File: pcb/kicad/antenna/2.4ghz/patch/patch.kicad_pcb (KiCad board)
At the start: 2 copper layers, 2 parts, among them P1 SMA

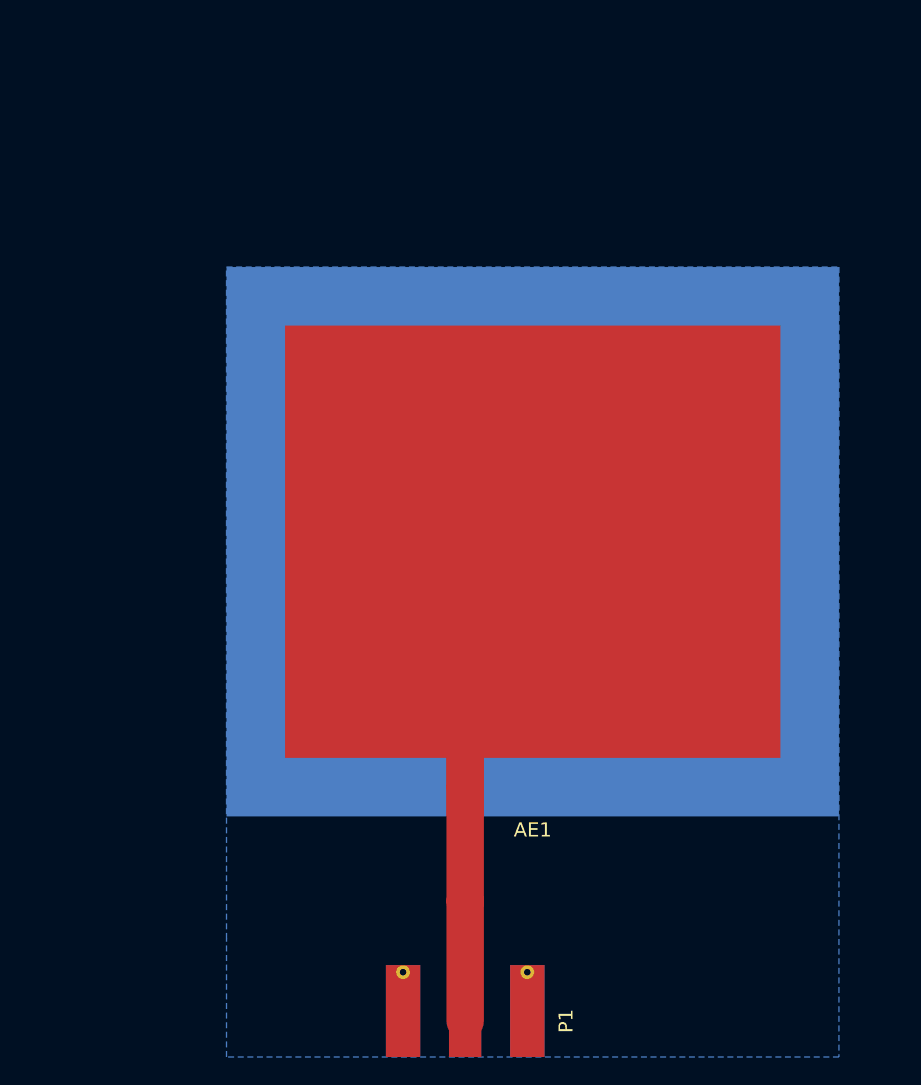
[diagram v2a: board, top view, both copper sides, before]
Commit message: Add new tests for patch antenna
Two new test boards laid out to test impedance and performance due to
the effect of larger copper void space in the presence of nearby ground
copper, one board with a matching circuit and the other without. Traces
no longer follow the optimal transmission line width for 50ohm
performance due to the use of 0402 SMD technology.
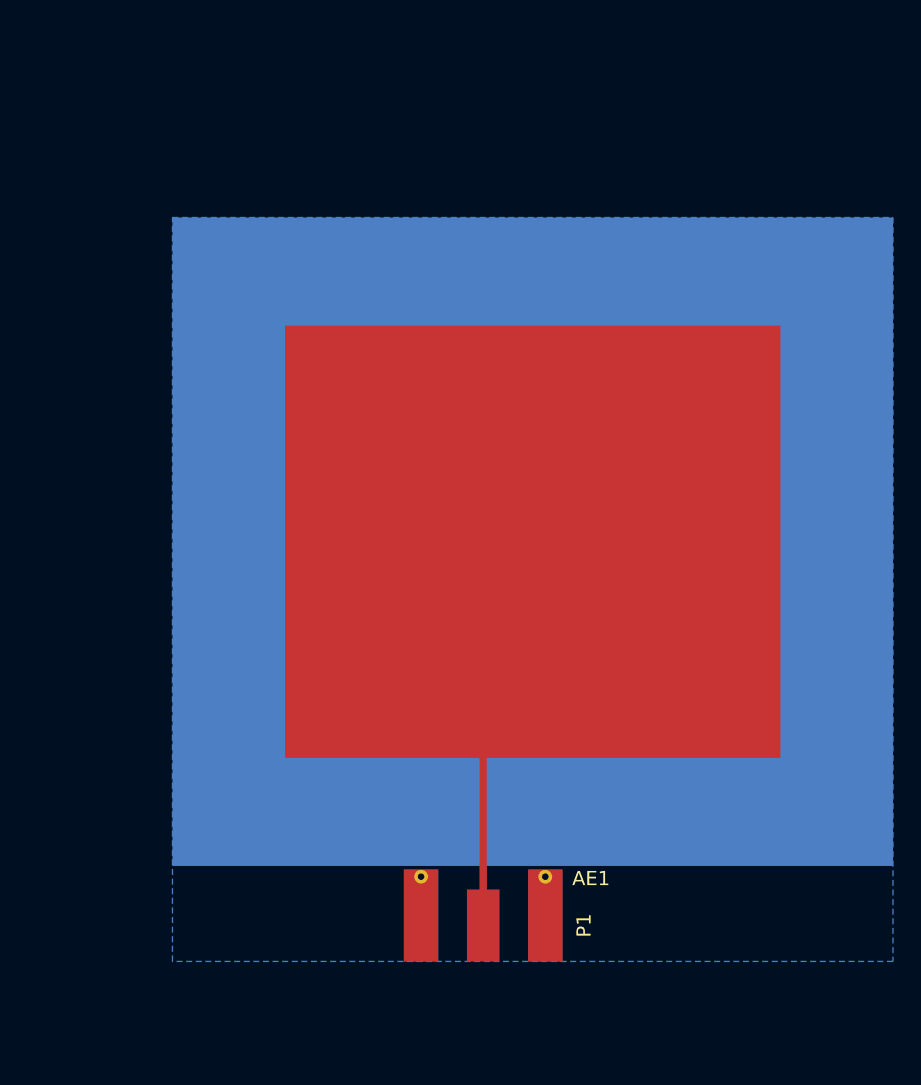
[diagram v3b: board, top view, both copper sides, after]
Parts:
- AE1: value Antenna -> Antenna_Shield
- moved P1 6.85 mm to (145.1, 114.2)
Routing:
- net /SIG: track 35.8 -> 28.5 mm
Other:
- net class Default: trace_width 2.6416 -> 0.508
- board text added: "April 4, 2017"
- board text removed: "March 15, 2017"
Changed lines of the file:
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@@
 (kicad_pcb (version 4) (host pcbnew 4.0.5)
   (general
-    (links 8)
+    (links 7)
     (no_connects 0)
-    (area 126.873 67.678 272.295714 194.39)
+    (area 0 0 0 0)
     (thickness 1.5748)
     (drawings 7)
-    (tracks 4)
+    (tracks 2)
     (zones 0)
     (modules 2)
@@
   )
   (setup
-    (last_trace_width 2.6416)
+    (last_trace_width 0.508)
     (trace_clearance 0.127)
     (zone_clearance 0.127)
@@
     (mod_text_size 1 1)
     (mod_text_width 0.15)
-    (pad_size 43.18 38.735)
+    (pad_size 34.925 30.48)
     (pad_drill 0)
     (pad_to_mask_clearance 0.2)
-    (aux_axis_origin 127 125.22962)
+    (aux_axis_origin 123.19 118.491)
     (visible_elements 7FFFFFFF)
     (pcbplotparams
@@
   (net_class Default "This is the default net class."
     (clearance 0.127)
-    (trace_width 2.6416)
+    (trace_width 0.508)
     (via_dia 0.3048)
     (via_drill 0.254)
@@
     (add_net GND)
   )
-  (module Antennas:Patch_Antenna_2.4GHz (layer F.Cu)
-    (at 148.59 88.9)
-    (descr "2.4GHz Patch Antenna")
-    (tags "antenna patch 2.4")
-    (fp_text reference AE1 (at 0 20.32) (layer F.SilkS)
-      (effects (font (size 1 1) (thickness 0.15)))
-    )
-    (fp_text value Antenna (at 0 -20.32) (layer F.Fab)
-      (effects (font (size 1 1) (thickness 0.15)))
-    )
-    (pad 2 smd rect (at 0 0) (size 43.18 38.735) (layers B.Cu)
-      (net 2 GND))
-    (pad 1 smd rect (at 0 0) (size 34.925 30.48) (layers F.Cu)
-      (net 1 /SIG))
-    (pad 1 smd rect (at -4.7625 17.30375) (size 2.6416 4.1275) (layers F.Cu)
-      (net 1 /SIG))
-  )
   (module Misc:Molex_SMA_Jack_Edge_Mount (layer F.Cu)
-    (at 143.8275 120.97004 90)
+    (at 145.0975 114.2365 90)
     (descr "Molex SMA Jack, Edge Mount")
     (tags "sma edge")
@@
       (net 2 GND) (zone_connect 2))
   )
-  (gr_line (start 170.18 69.5325) (end 127 69.5325) (angle 90) (layer Margin) (width 0.2))
-  (gr_line (start 170.18 125.22962) (end 170.18 69.5325) (angle 90) (layer Margin) (width 0.2))
-  (gr_line (start 127 125.22962) (end 170.18 125.22962) (angle 90) (layer Margin) (width 0.2))
-  (gr_line (start 127 69.5325) (end 127 125.22962) (angle 90) (layer Margin) (width 0.2))
-  (gr_text "March 15, 2017" (at 217.17 193.04) (layer Cmts.User)
+  (module Antennas:Patch_Antenna_2.4GHz (layer F.Cu)
+    (at 148.59 88.9)
+    (descr "2.4GHz Patch Antenna")
+    (tags "antenna patch 2.4")
+    (fp_text reference AE1 (at 4.1148 23.749) (layer F.SilkS)
+      (effects (font (size 1 1) (thickness 0.15)))
+    )
+    (fp_text value Antenna_Shield (at 0 -23.622) (layer F.Fab)
+      (effects (font (size 1 1) (thickness 0.15)))
+    )
+    (pad 2 smd rect (at 0 0) (size 50.8 45.72) (layers B.Cu)
+      (net 2 GND))
+    (pad 1 smd rect (at 0 0) (size 34.925 30.48) (layers F.Cu)
+      (net 1 /SIG))
+  )
+  (gr_line (start 173.99 66.04) (end 123.19 66.04) (angle 90) (layer Margin) (width 0.2))
+  (gr_line (start 173.99 118.491) (end 173.99 66.04) (angle 90) (layer Margin) (width 0.2))
+  (gr_line (start 123.19 118.491) (end 173.99 118.491) (angle 90) (layer Margin) (width 0.2))
+  (gr_line (start 123.19 66.04) (end 123.19 118.491) (angle 90) (layer Margin) (width 0.2))
+  (gr_text "April 4, 2017" (at 214.63 193.04) (layer Cmts.User)
     (effects (font (size 1.5 1.5) (thickness 0.3)))
   )
@@
     (effects (font (size 1.5 1.5) (thickness 0.3)))
   )
-  (segment (start 143.8275 122.69004) (end 143.8275 114.242) (width 2.6416) (layer F.Cu) (net 1) (status 400000))
-  (segment (start 143.8275 114.242) (end 143.8275 106.20375) (width 2.6416) (layer F.Cu) (net 1) (status 30))
-  (segment (start 143.8275 106.20375) (end 143.8275 93.6625) (width 2.6416) (layer F.Cu) (net 1) (status 30))
-  (segment (start 143.8275 93.6625) (end 148.59 88.9) (width 2.6416) (layer F.Cu) (net 1) (status 30))
+  (segment (start 145.0975 115.9565) (end 145.0975 92.3925) (width 0.508) (layer F.Cu) (net 1))
+  (segment (start 145.0975 92.3925) (end 148.59 88.9) (width 0.508) (layer F.Cu) (net 1))
   (zone (net 2) (net_name GND) (layer B.Cu) (hatch edge 0.508)
     (connect_pads thru_hole_only (clearance 0.127))
     (min_thickness 0.127)
-    (fill yes (arc_segments 32) (thermal_gap 0.508) (thermal_bridge_width 0.508))
+    (fill yes (arc_segments 16) (thermal_gap 0.508) (thermal_bridge_width 0.508))
     (polygon
       (pts
-        (xy 170.18 125.22962) (xy 127 125.22962) (xy 127 116.9035) (xy 127 69.5325) (xy 170.18 69.5325)
+        (xy 173.99 118.491) (xy 123.19 118.491) (xy 123.19 66.04) (xy 173.99 66.04)
       )
     )
-    (polygon
-      (pts        (xy 127 116.9035) (xy 127.00508 116.9162) (xy 127.00508 116.9035)
-      )
-    )

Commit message: Add gerbtool files for new patch tests
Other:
- board text added: "0.2.1"
- board text removed: "0.2"
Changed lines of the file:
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@@
     (links 7)
     (no_connects 0)
-    (area 0 0 0 0)
+    (area 123.063 64.376 272.295714 194.39)
     (thickness 1.5748)
     (drawings 7)
@@
     (effects (font (size 1.5 1.5) (thickness 0.3)))
   )
-  (gr_text 0.2 (at 270.51 193.04) (layer Cmts.User)
+  (gr_text 0.2.1 (at 271.78 193.04) (layer Cmts.User)
     (effects (font (size 1.5 1.5) (thickness 0.3)))
   )

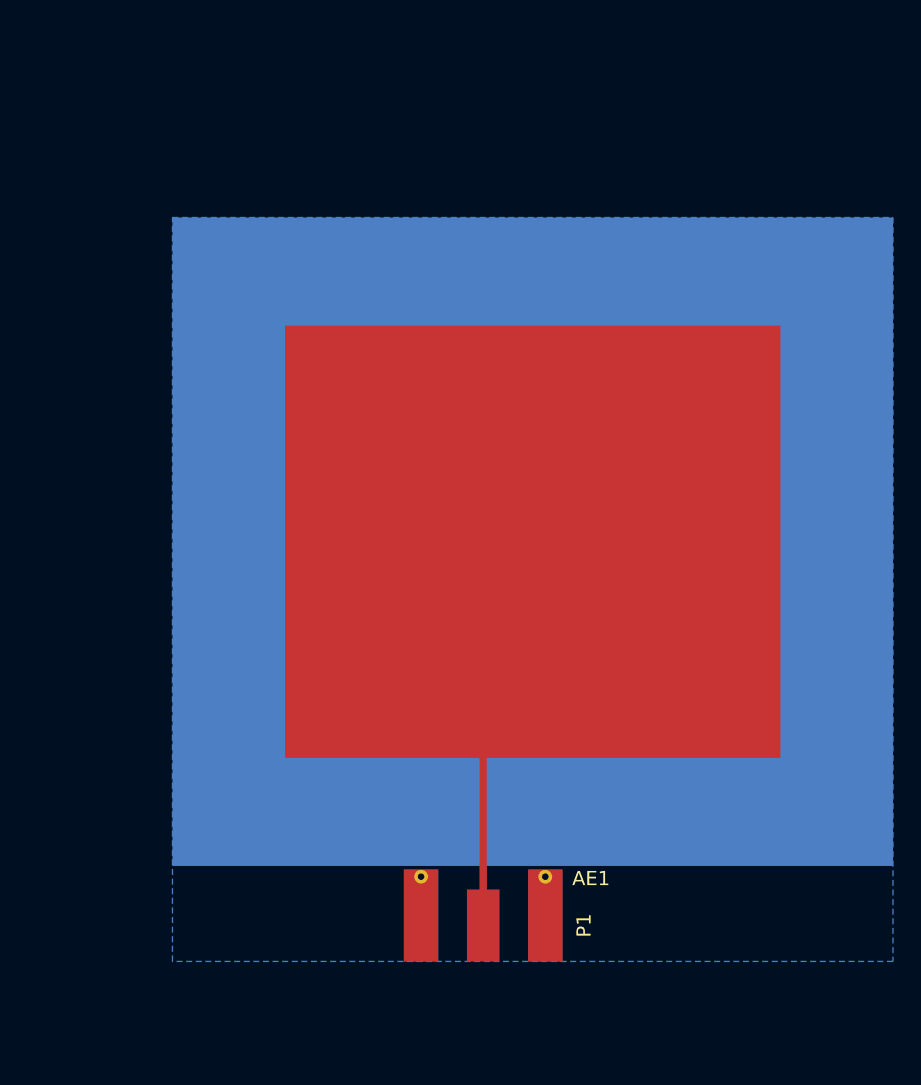
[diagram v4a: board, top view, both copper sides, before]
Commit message: Add patch antennas with transmission line matching
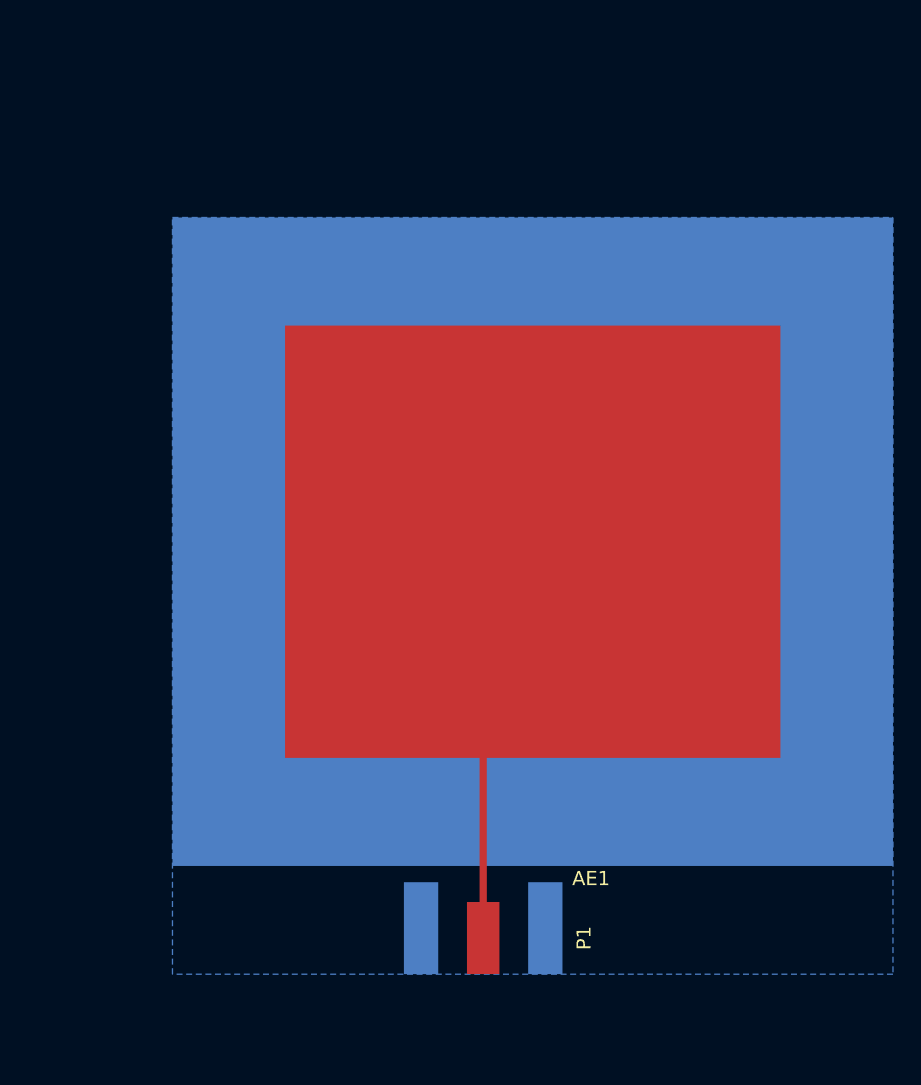
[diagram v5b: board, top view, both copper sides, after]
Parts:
- moved P1 0.89 mm to (145.1, 115.1)
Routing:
- net /SIG: track 28.5 -> 34.3 mm
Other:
- rule pad_to_mask_clearance: 0.2 -> 0.0762
- board text added: "0.3"
- board text added: "April 28, 2017"
- board text removed: "0.2.1"
- board text removed: "April 4, 2017"
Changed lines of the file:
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@@
 (kicad_pcb (version 4) (host pcbnew 4.0.5)
   (general
-    (links 7)
+    (links 3)
     (no_connects 0)
-    (area 123.063 64.376 272.295714 194.39)
+    (area 123.063 64.376 273.565714 194.39)
     (thickness 1.5748)
     (drawings 7)
-    (tracks 2)
+    (tracks 3)
     (zones 0)
     (modules 2)
@@
     (last_trace_width 0.508)
     (trace_clearance 0.127)
-    (zone_clearance 0.127)
+    (zone_clearance 0.1524)
     (zone_45_only yes)
     (trace_min 0.127)
@@
     (pad_size 34.925 30.48)
     (pad_drill 0)
-    (pad_to_mask_clearance 0.2)
-    (aux_axis_origin 123.19 118.491)
+    (pad_to_mask_clearance 0.0762)
+    (aux_axis_origin 123.19 119.3927)
     (visible_elements 7FFFFFFF)
     (pcbplotparams
@@
   )
   (module Misc:Molex_SMA_Jack_Edge_Mount (layer F.Cu)
-    (at 145.0975 114.2365 90)
+    (at 145.0975 115.1255 90)
     (descr "Molex SMA Jack, Edge Mount")
     (tags "sma edge")
@@
     (pad 1 smd rect (at -1.72 0 90) (size 5.08 2.29) (layers F.Cu F.Paste F.Mask)
       (net 1 /SIG))
-    (pad 2 smd rect (at -1.02 -4.38 90) (size 6.48 2.42) (layers F.Cu F.Paste F.Mask)
-      (net 2 GND))
-    (pad 2 smd rect (at -1.02 4.38 90) (size 6.48 2.42) (layers F.Cu F.Paste F.Mask)
-      (net 2 GND))
     (pad 2 smd rect (at -1.02 -4.38 90) (size 6.48 2.42) (layers B.Cu B.Paste B.Mask)
       (net 2 GND))
     (pad 2 smd rect (at -1.02 4.38 90) (size 6.48 2.42) (layers B.Cu B.Paste B.Mask)
       (net 2 GND))
-    (pad 2 thru_hole circle (at 1.72 -4.38 90) (size 0.97 0.97) (drill 0.46) (layers *.Cu)
-      (net 2 GND) (zone_connect 2))
-    (pad 2 thru_hole circle (at 1.72 4.38 90) (size 0.97 0.97) (drill 0.46) (layers *.Cu)
-      (net 2 GND) (zone_connect 2))
   )
   (module Antennas:Patch_Antenna_2.4GHz (layer F.Cu)
@@
   )
   (gr_line (start 173.99 66.04) (end 123.19 66.04) (angle 90) (layer Margin) (width 0.2))
-  (gr_line (start 173.99 118.491) (end 173.99 66.04) (angle 90) (layer Margin) (width 0.2))
-  (gr_line (start 123.19 118.491) (end 173.99 118.491) (angle 90) (layer Margin) (width 0.2))
-  (gr_line (start 123.19 66.04) (end 123.19 118.491) (angle 90) (layer Margin) (width 0.2))
-  (gr_text "April 4, 2017" (at 214.63 193.04) (layer Cmts.User)
+  (gr_line (start 173.99 119.3927) (end 173.99 66.04) (angle 90) (layer Margin) (width 0.2))
+  (gr_line (start 123.19 119.3927) (end 173.99 119.3927) (angle 90) (layer Margin) (width 0.2))
+  (gr_line (start 123.19 66.04) (end 123.19 119.3927) (angle 90) (layer Margin) (width 0.2))
+  (gr_text "April 28, 2017" (at 215.9 193.04) (layer Cmts.User)
     (effects (font (size 1.5 1.5) (thickness 0.3)))
   )
-  (gr_text 0.2.1 (at 271.78 193.04) (layer Cmts.User)
+  (gr_text 0.3 (at 271.78 193.04) (layer Cmts.User)
     (effects (font (size 1.5 1.5) (thickness 0.3)))
   )
@@
     (effects (font (size 1.5 1.5) (thickness 0.3)))
   )
-  (segment (start 145.0975 115.9565) (end 145.0975 92.3925) (width 0.508) (layer F.Cu) (net 1))
+  (segment (start 145.0975 116.8455) (end 145.0975 92.3925) (width 0.508) (layer F.Cu) (net 1))
+  (segment (start 145.0975 92.3925) (end 148.59 88.9) (width 0.508) (layer F.Cu) (net 1))
   (segment (start 145.0975 92.3925) (end 148.59 88.9) (width 0.508) (layer F.Cu) (net 1))
   (zone (net 2) (net_name GND) (layer B.Cu) (hatch edge 0.508)
-    (connect_pads thru_hole_only (clearance 0.127))
-    (min_thickness 0.127)
+    (connect_pads thru_hole_only (clearance 0.1524))
+    (min_thickness 0.1524)
     (fill yes (arc_segments 16) (thermal_gap 0.508) (thermal_bridge_width 0.508))
     (polygon
       (pts
-        (xy 173.99 118.491) (xy 123.19 118.491) (xy 123.19 66.04) (xy 173.99 66.04)
+        (xy 173.99 119.3927) (xy 123.19 119.3927) (xy 123.19 66.04) (xy 173.99 66.04)
       )
     )
+  )
+  (zone (net 0) (net_name "") (layer F.Mask) (hatch edge 0.508)
+    (connect_pads thru_hole_only (clearance 0.1524))
+    (min_thickness 0.0762)
+    (fill yes (arc_segments 16) (thermal_gap 0.508) (thermal_bridge_width 0.508))
+    (polygon
+      (pts
+        (xy 173.99 119.3927) (xy 123.19 119.3927) (xy 123.19 66.04) (xy 173.99 66.04)
+      )
+    )
